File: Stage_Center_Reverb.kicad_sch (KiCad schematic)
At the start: 48 parts, among them J1 Input, J2 Output, J3 ToTank, J4 FromTank, J6 Conn_01x03, J7 Conn_01x03, SW1 SW_SPDT, SW2 SW_SPDT, SW3 SW_SPDT, SW4 kill, U1 TL072, U2 TL072, U4 L78L15, U5 L79L15

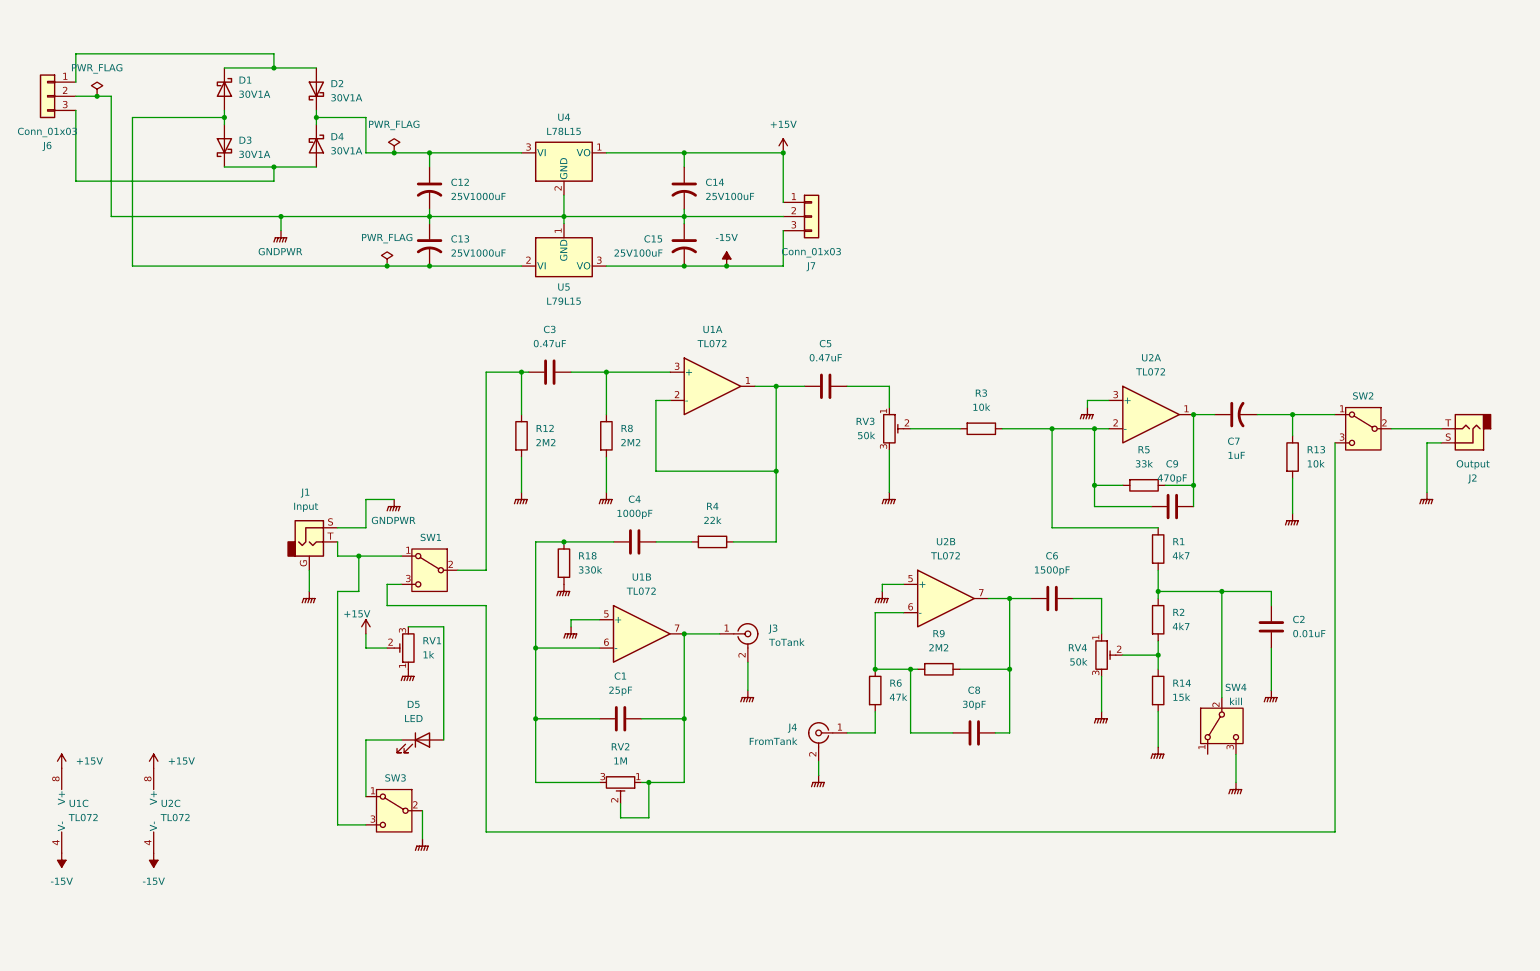
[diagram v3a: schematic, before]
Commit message: 電源をトランスから正負15Vを作るように変更 コネクタ等との接続をXHコネクタを使うよう変更
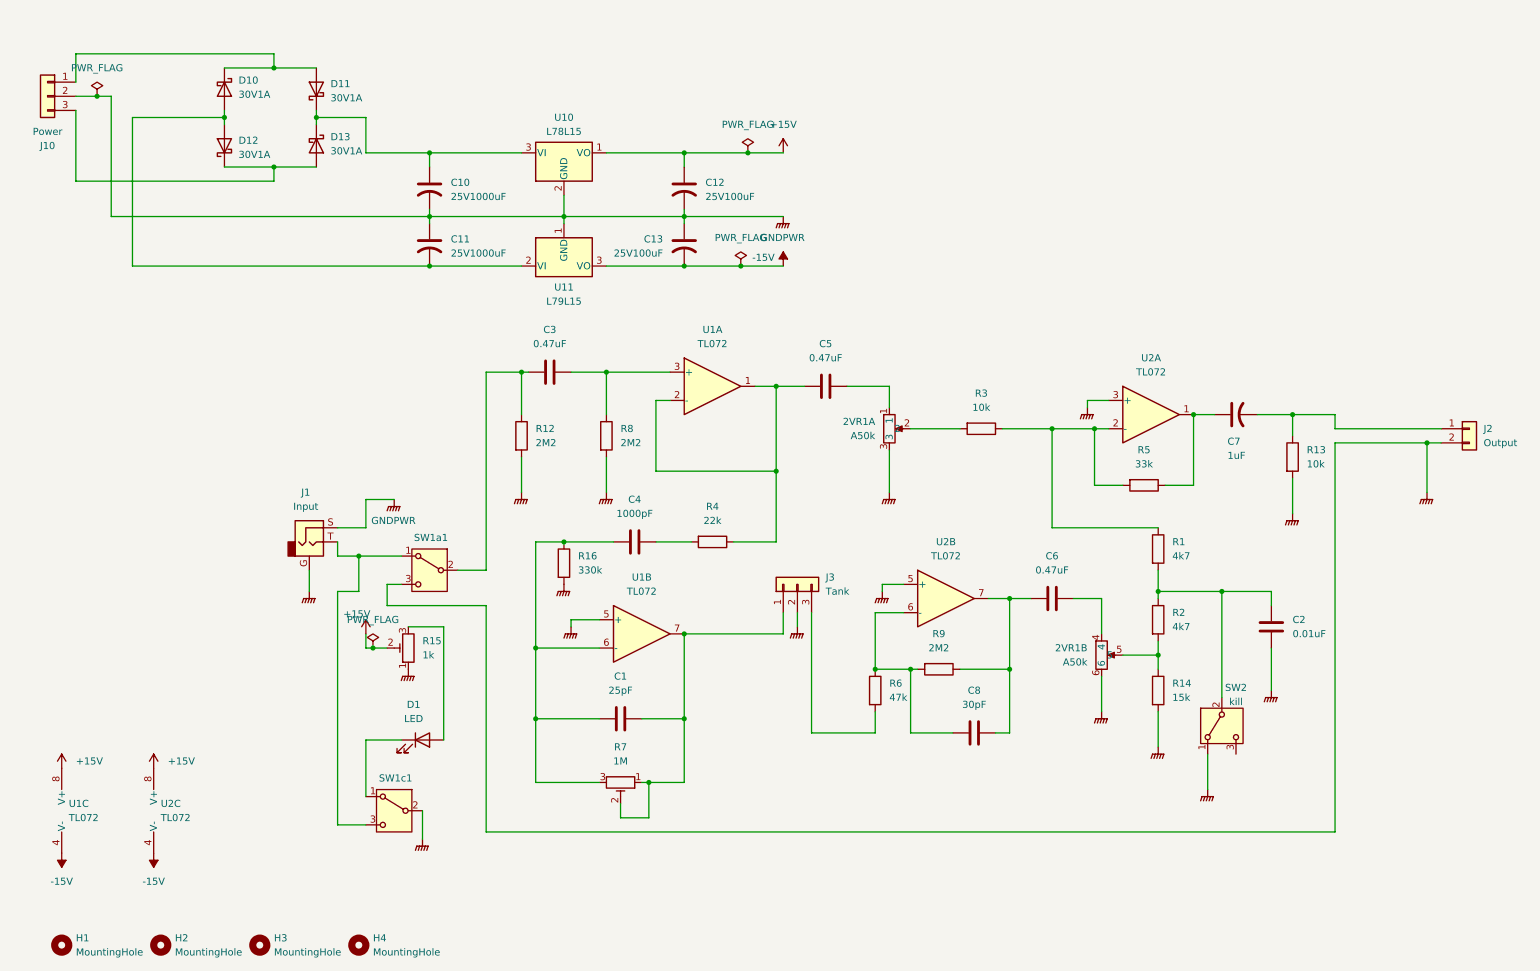
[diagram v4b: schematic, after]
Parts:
- removed C9: 470pF, Capacitor_THT:C_Disc_D5.0mm_W2.5mm_P5.00mm, symbol Device:C
- removed J2: Output, symbol Connector_Audio:AudioJack2
- removed J3: ToTank, symbol Connector:Conn_Coaxial
- removed J4: FromTank, symbol Connector:Conn_Coaxial
- removed J7: Conn_01x03, Connector_JST:JST_XH_B3B-XH-A_1x03_P2.50mm_Vertical, symbol Connector_Generic:Conn_01x03
- removed RV3, RV4: 50k, symbol Device:R_Potentiometer_Trim
- removed SW2: SW_SPDT, symbol Switch:SW_SPDT
- added 2VR1: A50k, Connector_JST:JST_XH_B5B-XH-A_1x05_P2.50mm_Vertical, symbol @MyLibrary:double_vr
- added H1, H2, H3, H4: MountingHole, MountingHole:MountingHole_3.2mm_M3, symbol Mechanical:MountingHole
- added J2: Output, Connector_JST:JST_XH_B2B-XH-A_1x02_P2.50mm_Vertical, symbol Connector_Generic:Conn_01x02
- added J3: Tank, Connector_JST:JST_XH_B3B-XH-A_1x03_P2.50mm_Vertical, symbol Connector_Generic:Conn_01x03
- C6: value 1500pF -> 0.47uF
- J10: renamed from J6; value Conn_01x03 -> Power
- R16: renamed from R18; footprint Resistor_THT:R_Axial_DIN0207_L6.3mm_D2.5mm_P7.62mm_Horizontal -> Resistor_THT:R_Axial_DIN0207_L6.3mm_D2.5mm_P10.16mm_Horizontal
- SW2: renamed from SW4; footprint (none) -> Connector_JST:JST_XH_B2B-XH-A_1x02_P2.50mm_Vertical
- U1, U2: footprint (none) -> Package_DIP:DIP-8_W7.62mm_Socket
- renumbered C12 to C10, C13 to C11, C14 to C12, C15 to C13, D5 to D1, D1 to D10, D2 to D11, D3 to D12, D4 to D13, RV1 to R15, RV2 to R7, SW1 to SW1a1, SW3 to SW1c1, U4 to U10, U5 to U11
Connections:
- net GNDPWR: now also SW1a1.3 (C), SW2.1 (A), 2VR1.3, 2VR1.6, J2.2 (Pin_2), J3.2 (Pin_2); no longer SW2.3 (C)
- net at C6.2: now also 2VR1.4
- net at R14.1, R2.2: now also 2VR1.5
- net at R6.2: now also J3.3 (Pin_3)
- net at C5.2: now also 2VR1.1
- net at C7.2, R13.1: now also J2.1 (Pin_1)
- net at C1.2, R7.1, R7.2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: now also J3.1 (Pin_1)
- net at R3.2: now also 2VR1.2

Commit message: 電元部分の電解コンデンサを35Vに変更 ICを抜きやすいよう配置を修正
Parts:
- C10, C11: value 25V1000uF -> 35V1000uF; footprint Capacitor_THT:CP_Radial_D10.0mm_P5.00mm -> Capacitor_THT:CP_Radial_D12.5mm_P5.00mm
- renumbered R15 to VR15, R7 to VR7
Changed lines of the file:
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@@
 			)
 		)
-		(property "Value" "25V1000uF"
+		(property "Value" "35V1000uF"
 			(at 96.52 57.4039 0)
 			(effects
@@
 			)
 		)
-		(property "Footprint" "Capacitor_THT:CP_Radial_D10.0mm_P5.00mm"
+		(property "Footprint" "Capacitor_THT:CP_Radial_D12.5mm_P5.00mm"
 			(at 92.71 55.88 0)
 			(effects
@@
 		(dnp no)
 		(fields_autoplaced yes)
-		(property "Reference" "R7"
+		(property "Reference" "VR7"
 			(at 127 146.05 90)
 			(effects
@@
 			(project ""
 				(path "/bb175fc0-f13d-4415-8630-2bbdc9c8566e"
-					(reference "R7")
+					(reference "VR7")
 					(unit 1)
 				)
@@
 		(on_board yes)
 		(dnp no)
-		(property "Reference" "R15"
+		(property "Reference" "VR15"
 			(at 91.44 126.9999 0)
 			(effects
@@
 			(project ""
 				(path "/bb175fc0-f13d-4415-8630-2bbdc9c8566e"
-					(reference "R15")
+					(reference "VR15")
 					(unit 1)
 				)
@@
 			)
 		)
-		(property "Value" "25V1000uF"
+		(property "Value" "35V1000uF"
 			(at 96.52 47.2439 0)
 			(effects
@@
 			)
 		)
-		(property "Footprint" "Capacitor_THT:CP_Radial_D10.0mm_P5.00mm"
+		(property "Footprint" "Capacitor_THT:CP_Radial_D12.5mm_P5.00mm"
 			(at 92.71 45.72 0)
 			(effects

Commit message: LED周りの修正
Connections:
- net +15V: now also VR15.1; no longer VR15.2
- net GNDPWR: no longer VR15.1
- net at D1.2 (A), VR15.3: now also VR15.2
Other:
- moved on the sheet: VR15
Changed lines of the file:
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@@
 	)
 	(junction
+		(at 95.25 128.27)
+		(diameter 0)
+		(color 0 0 0 0)
+	)
+	(junction
 		(at 196.85 132.08)
 		(diameter 0)
@@
 	(wire
 		(pts
+			(xy 92.71 128.27) (xy 95.25 128.27)
+		)
+		(stroke
+			(width 0)
+			(type default)
+		)
+	)
+	(wire
+		(pts
 			(xy 186.69 143.51) (xy 179.07 143.51)
 		)
@@
 	(wire
 		(pts
-			(xy 95.25 124.46) (xy 95.25 144.78)
+			(xy 95.25 124.46) (xy 95.25 128.27)
 		)
 		(stroke
@@
 	(wire
 		(pts
+			(xy 95.25 128.27) (xy 95.25 144.78)
+		)
+		(stroke
+			(width 0)
+			(type default)
+		)
+	)
+	(wire
+		(pts
 			(xy 154.94 96.52) (xy 154.94 81.28)
 		)
@@
 	(symbol
 		(lib_id "power:GNDPWR")
-		(at 88.9 132.08 0)
-		(unit 1)
-		(exclude_from_sim no)
-		(in_bom yes)
-		(on_board yes)
-		(dnp no)
-		(fields_autoplaced yes)
-		(property "Reference" "#PWR02"
-			(at 88.9 137.16 0)
-			(effects
-				(font
-					(size 1.27 1.27)
-				)
-				(hide yes)
-			)
-		)
-		(property "Value" "GNDPWR"
-			(at 88.773 135.89 0)
-			(effects
-				(font
-					(size 1.27 1.27)
-				)
-				(hide yes)
-			)
-		)
-		(property "Footprint" ""
-			(at 88.9 133.35 0)
-			(effects
-				(font
-					(size 1.27 1.27)
-				)
-				(hide yes)
-			)
-		)
-		(property "Datasheet" ""
-			(at 88.9 133.35 0)
-			(effects
-				(font
-					(size 1.27 1.27)
-				)
-				(hide yes)
-			)
-		)
-		(property "Description" "Power symbol creates a global label with name \"GNDPWR\" , global ground"
-			(at 88.9 132.08 0)
-			(effects
-				(font
-					(size 1.27 1.27)
-				)
-				(hide yes)
-			)
-		)
-		(pin "1"
-		)
-		(instances
-			(project "Stage_Center_Reverb"
-				(path "/bb175fc0-f13d-4415-8630-2bbdc9c8566e"
-					(reference "#PWR02")
-					(unit 1)
-				)
-			)
-		)
-	)
-	(symbol
-		(lib_id "power:GNDPWR")
 		(at 116.84 116.84 0)
 		(unit 1)
@@
 	(symbol
 		(lib_id "Device:R_Potentiometer_Trim")
-		(at 88.9 128.27 180)
+		(at 88.9 128.27 90)
 		(unit 1)
 		(exclude_from_sim no)
@@
 		(dnp no)
 		(property "Reference" "VR15"
-			(at 91.44 126.9999 0)
+			(at 90.1701 130.81 0)
 			(effects
 				(font
@@
 		)
 		(property "Value" "1k"
-			(at 91.44 129.5399 0)
+			(at 87.6301 130.81 0)
 			(effects
 				(font

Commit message: 回路図上トゥルーバイパスがグランドに落ちていたのを修正
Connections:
- net GNDPWR: no longer SW1a1.3 (C)
- net at C7.2, J2.1 (Pin_1), R13.1: now also SW1a1.3 (C)
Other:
- moved on the sheet: J2
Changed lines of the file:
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@@
+	)
+	(junction
+		(at 255.27 86.36)
+		(diameter 0)
+		(color 0 0 0 0)
 	)
 	(junction
@@
 	)
 	(junction
-		(at 271.78 91.44)
-		(diameter 0)
-		(color 0 0 0 0)
-	)
-	(junction
 		(at 247.65 86.36)
 		(diameter 0)
@@
 	(wire
 		(pts
-			(xy 271.78 91.44) (xy 271.78 100.33)
+			(xy 271.78 88.9) (xy 271.78 100.33)
 		)
 		(stroke
@@
 	(wire
 		(pts
-			(xy 274.32 91.44) (xy 271.78 91.44)
+			(xy 274.32 88.9) (xy 271.78 88.9)
 		)
 		(stroke
@@
 	(wire
 		(pts
+			(xy 255.27 86.36) (xy 255.27 161.29)
+		)
+		(stroke
+			(width 0)
+			(type default)
+		)
+	)
+	(wire
+		(pts
 			(xy 161.29 143.51) (xy 172.72 143.51)
 		)
@@
 	(wire
 		(pts
-			(xy 255.27 88.9) (xy 274.32 88.9)
+			(xy 255.27 86.36) (xy 274.32 86.36)
 		)
 		(stroke
@@
 	(wire
 		(pts
-			(xy 255.27 88.9) (xy 255.27 86.36)
-		)
-		(stroke
-			(width 0)
-			(type default)
-		)
-	)
-	(wire
-		(pts
 			(xy 138.43 50.8) (xy 156.21 50.8)
 		)
@@
 	(wire
 		(pts
-			(xy 255.27 91.44) (xy 271.78 91.44)
-		)
-		(stroke
-			(width 0)
-			(type default)
-		)
-	)
-	(wire
-		(pts
 			(xy 124.46 59.69) (xy 138.43 59.69)
 		)
@@
 		(pts
 			(xy 39.37 33.02) (xy 39.37 59.69)
-		)
-		(stroke
-			(width 0)
-			(type default)
-		)
-	)
-	(wire
-		(pts
-			(xy 255.27 91.44) (xy 255.27 161.29)
 		)
 		(stroke
@@
 	(symbol
 		(lib_id "Connector_Generic:Conn_01x02")
-		(at 279.4 88.9 0)
+		(at 279.4 86.36 0)
 		(unit 1)
 		(exclude_from_sim no)
@@
 		(fields_autoplaced yes)
 		(property "Reference" "J2"
+			(at 281.94 86.3599 0)
+			(effects
+				(font
+					(size 1.27 1.27)
+				)
+				(justify left)
+			)
+		)
+		(property "Value" "Output"
 			(at 281.94 88.8999 0)
 			(effects
@@
 			)
 		)
-		(property "Value" "Output"
-			(at 281.94 91.4399 0)
-			(effects
-				(font
-					(size 1.27 1.27)
-				)
-				(justify left)
-			)
-		)
 		(property "Footprint" "Connector_JST:JST_XH_B2B-XH-A_1x02_P2.50mm_Vertical"
-			(at 279.4 88.9 0)
+			(at 279.4 86.36 0)
 			(effects
 				(font
@@
 		)
 		(property "Datasheet" "~"
-			(at 279.4 88.9 0)
+			(at 279.4 86.36 0)
 			(effects
 				(font
@@
 		)
 		(property "Description" "Generic connector, single row, 01x02, script generated (kicad-library-utils/schlib/autogen/connector/)"
-			(at 279.4 88.9 0)
-			(effects
-				(font
+			(at 279.4 86.36 0)
+			(effects
+				(font

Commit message: C4,R6のハイパスフィルタのカットオフ周波数をを下げた
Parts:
- C4: value 1000pF -> 1500pF
- R16: value 330k -> 560k
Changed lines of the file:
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@@
 			)
 		)
-		(property "Value" "330k"
+		(property "Value" "560k"
 			(at 119.38 114.2999 0)
 			(effects
@@
 			)
 		)
-		(property "Value" "1000pF"
+		(property "Value" "1500pF"
 			(at 129.54 104.14 90)
 			(effects
